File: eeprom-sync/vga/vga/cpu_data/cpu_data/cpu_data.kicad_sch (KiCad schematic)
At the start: 32 parts, among them J1 Conn_02x06_Odd_Even, J10 Conn_01x03_Female, J11 Conn_01x02_Female, J12 Conn_02x05_Odd_Even, J2 Conn_01x02_Female, J3 Conn_01x04_Female, J4 Conn_01x15_Female, J5 Conn_01x15_Female, J6 Conn_02x08_Odd_Even, J7 Conn_01x02_Female, J8 Conn_01x02_Female, J9 Conn_01x08_Female, U1 GAL22V10, U2 74HC14, U3 74LS02, U4 IDT7205L12JG, U5 74LS573

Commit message: routing completed
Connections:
- net CS: now also J1.4 (Pin_4); no longer J1.3 (Pin_3)
- net GND: now also J1.1 (Pin_1), J1.11 (Pin_11), J1.3 (Pin_3), J1.5 (Pin_5), J1.7 (Pin_7), J1.9 (Pin_9); no longer J1.10 (Pin_10), J1.12 (Pin_12), J1.2 (Pin_2), J1.4 (Pin_4), J1.6 (Pin_6), J1.8 (Pin_8)
- net SCLK: now also J1.10 (Pin_10); no longer J1.9 (Pin_9)
- net SIO0: now also J1.12 (Pin_12); no longer J1.11 (Pin_11)
- net SIO1: now also J1.2 (Pin_2); no longer J1.1 (Pin_1)
- net SIO2: now also J1.8 (Pin_8); no longer J1.7 (Pin_7)
- net SIO3: now also J1.6 (Pin_6); no longer J1.5 (Pin_5)
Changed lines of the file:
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@@
   (junction (at 116.84 109.22) (diameter 0) (color 0 0 0 0)
   )
-  (junction (at 13.97 107.95) (diameter 0) (color 0 0 0 0)
+  (junction (at 26.67 107.95) (diameter 0) (color 0 0 0 0)
   )
   (junction (at 167.64 148.59) (diameter 0) (color 0 0 0 0)
@@
   (junction (at 90.17 107.95) (diameter 0) (color 0 0 0 0)
   )
-  (junction (at 13.97 105.41) (diameter 0) (color 0 0 0 0)
-  )
-  (junction (at 13.97 110.49) (diameter 0) (color 0 0 0 0)
+  (junction (at 26.67 105.41) (diameter 0) (color 0 0 0 0)
+  )
+  (junction (at 26.67 110.49) (diameter 0) (color 0 0 0 0)
   )
   (junction (at 200.66 148.59) (diameter 0) (color 0 0 0 0)
   )
-  (junction (at 13.97 115.57) (diameter 0) (color 0 0 0 0)
-  )
-  (junction (at 13.97 113.03) (diameter 0) (color 0 0 0 0)
+  (junction (at 26.67 115.57) (diameter 0) (color 0 0 0 0)
+  )
+  (junction (at 26.67 113.03) (diameter 0) (color 0 0 0 0)
   )
   (junction (at 167.64 143.51) (diameter 0) (color 0 0 0 0)
@@
     (stroke (width 0) (type default) (color 0 0 0 0))
   )
-  (wire (pts (xy 13.97 105.41) (xy 13.97 107.95))
+  (wire (pts (xy 26.67 105.41) (xy 26.67 107.95))
     (stroke (width 0) (type default) (color 0 0 0 0))
   )
@@
     (stroke (width 0) (type default) (color 0 0 0 0))
   )
-  (wire (pts (xy 13.97 110.49) (xy 13.97 113.03))
+  (wire (pts (xy 26.67 110.49) (xy 26.67 113.03))
     (stroke (width 0) (type default) (color 0 0 0 0))
   )
@@
     (stroke (width 0) (type default) (color 0 0 0 0))
   )
-  (wire (pts (xy 13.97 107.95) (xy 13.97 110.49))
+  (wire (pts (xy 26.67 107.95) (xy 26.67 110.49))
     (stroke (width 0) (type default) (color 0 0 0 0))
   )
@@
     (stroke (width 0) (type default) (color 0 0 0 0))
   )
-  (wire (pts (xy 13.97 113.03) (xy 13.97 115.57))
+  (wire (pts (xy 26.67 113.03) (xy 26.67 115.57))
     (stroke (width 0) (type default) (color 0 0 0 0))
   )
@@
     (stroke (width 0) (type default) (color 0 0 0 0))
   )
-  (wire (pts (xy 13.97 102.87) (xy 13.97 105.41))
+  (wire (pts (xy 26.67 102.87) (xy 26.67 105.41))
     (stroke (width 0) (type default) (color 0 0 0 0))
   )
@@
     (effects (font (size 1.27 1.27)) (justify left bottom))
   )
-  (label "SIO0" (at 26.67 115.57 0)
+  (label "SIO0" (at 13.97 115.57 0)
     (effects (font (size 1.27 1.27)) (justify left bottom))
   )
@@
     (effects (font (size 1.27 1.27)) (justify right bottom))
   )
-  (label "SIO2" (at 26.67 110.49 0)
+  (label "SIO2" (at 13.97 110.49 0)
     (effects (font (size 1.27 1.27)) (justify left bottom))
   )
@@
     (effects (font (size 1.27 1.27)) (justify right bottom))
   )
-  (label "SIO1" (at 26.67 102.87 0)
-    (effects (font (size 1.27 1.27)) (justify left bottom))
-  )
-  (label "SCLK" (at 26.67 113.03 0)
+  (label "SIO1" (at 13.97 102.87 0)
+    (effects (font (size 1.27 1.27)) (justify left bottom))
+  )
+  (label "SCLK" (at 13.97 113.03 0)
     (effects (font (size 1.27 1.27)) (justify left bottom))
   )
@@
     (effects (font (size 1.27 1.27)) (justify left bottom))
   )
-  (label "SIO3" (at 26.67 107.95 0)
+  (label "SIO3" (at 13.97 107.95 0)
     (effects (font (size 1.27 1.27)) (justify left bottom))
   )
@@
     (effects (font (size 1.27 1.27)) (justify left bottom))
   )
-  (label "CS" (at 26.67 105.41 0)
+  (label "CS" (at 13.97 105.41 0)
     (effects (font (size 1.27 1.27)) (justify left bottom))
   )
@@
     (pin "2")
   )
-  (symbol (lib_id "power:GND") (at 13.97 115.57 0) (unit 1)
-    (in_bom yes) (on_board yes) (fields_autoplaced)
-    (property "Reference" "#PWR0104" (id 0) (at 13.97 121.92 0)
-      (effects (font (size 1.27 1.27)) hide)
-    )
-    (property "Value" "GND" (id 1) (at 13.97 120.65 0))
-    (property "Footprint" "" (id 2) (at 13.97 115.57 0)
-      (effects (font (size 1.27 1.27)) hide)
-    )
-    (property "Datasheet" "" (id 3) (at 13.97 115.57 0)
-      (effects (font (size 1.27 1.27)) hide)
-    )
+  (symbol (lib_id "power:GND") (at 26.67 115.57 0) (unit 1)
+    (in_bom yes) (on_board yes) (fields_autoplaced)
+    (property "Reference" "#PWR0104" (id 0) (at 26.67 121.92 0)
+      (effects (font (size 1.27 1.27)) hide)
+    )
+    (property "Value" "GND" (id 1) (at 26.67 120.65 0))
+    (property "Footprint" "" (id 2) (at 26.67 115.57 0)
+      (effects (font (size 1.27 1.27)) hide)
+    )
+    (property "Datasheet" "" (id 3) (at 26.67 115.57 0)
+      (effects (font (size 1.27 1.27)) hide)
+    )

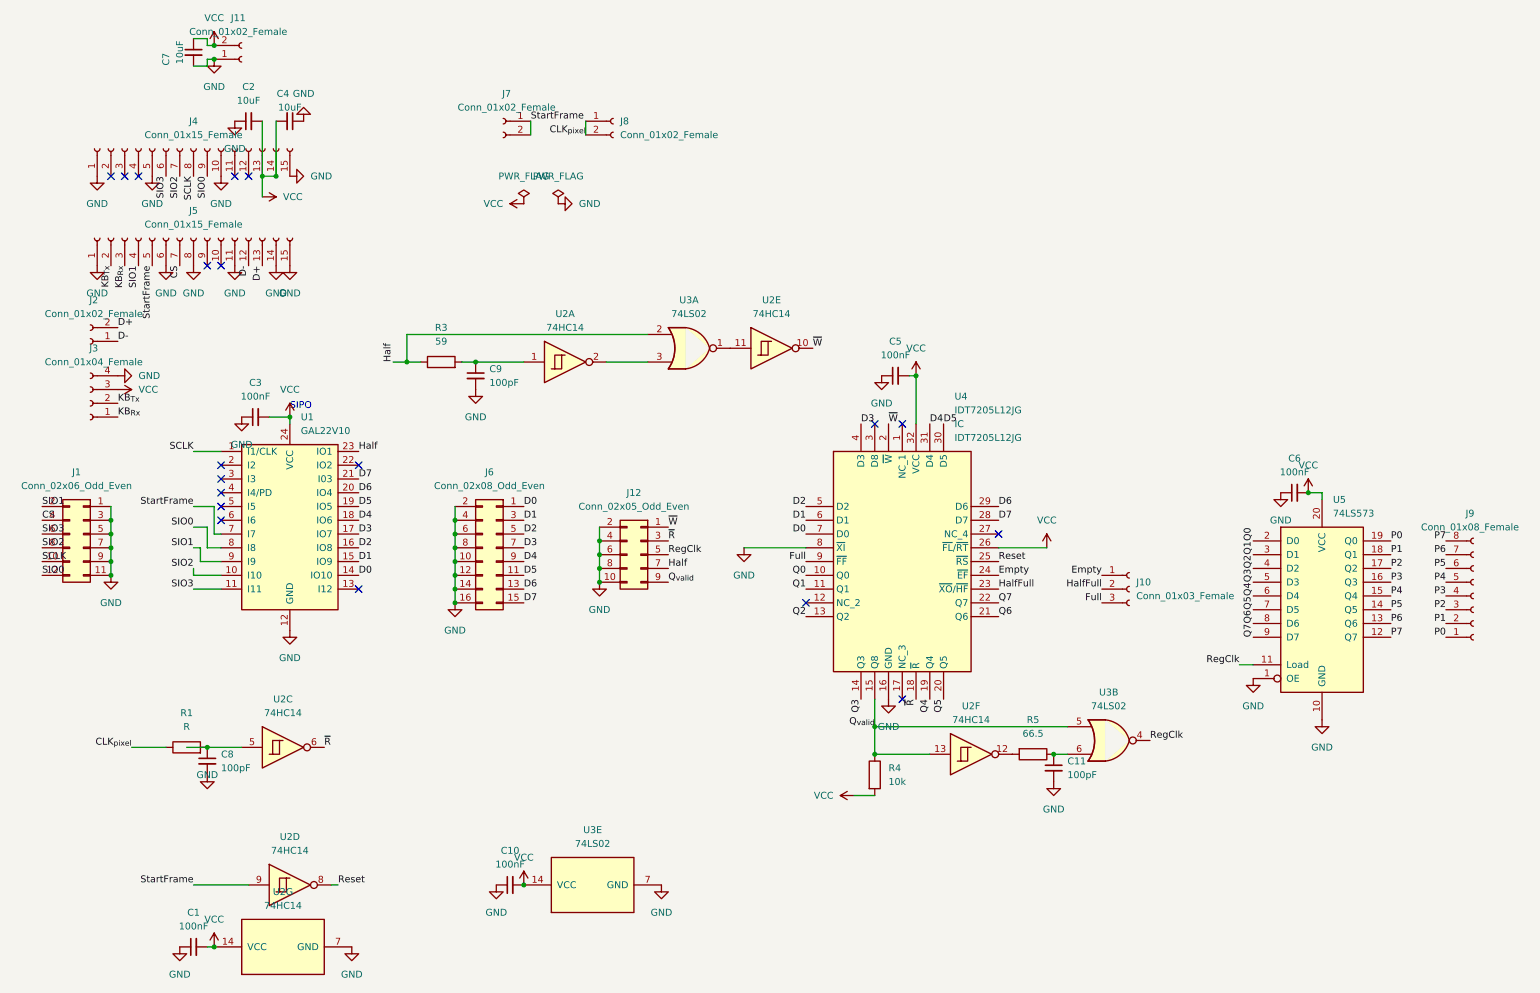
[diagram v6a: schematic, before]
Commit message: labels on the back of the board, layout and retraced, labels on front of board
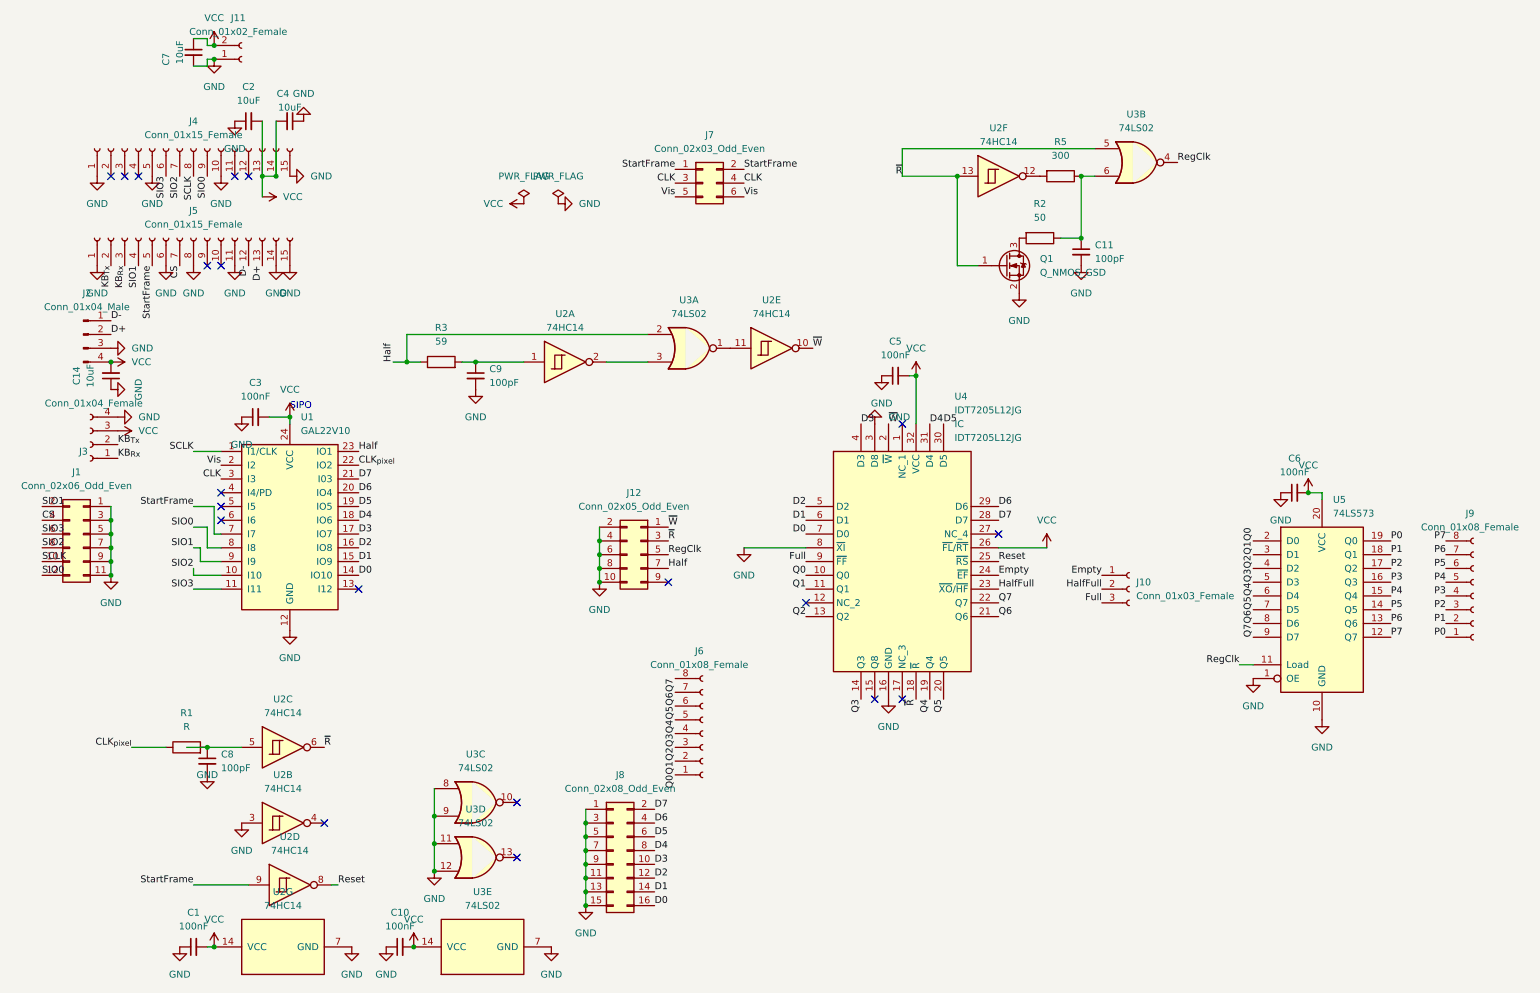
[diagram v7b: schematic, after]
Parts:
- removed J2: Conn_01x02_Female, Connector_PinHeader_2.54mm:PinHeader_1x02_P2.54mm_Vertical, symbol Connector:Conn_01x02_Female
- removed J6: Conn_02x08_Odd_Even, Connector_PinHeader_2.54mm:PinHeader_2x08_P2.54mm_Vertical, symbol Connector_Generic:Conn_02x08_Odd_Even
- removed J7, J8: Conn_01x02_Female, Connector_PinSocket_2.54mm:PinSocket_1x02_P2.54mm_Vertical, symbol Connector:Conn_01x02_Female
- removed R4: 10k, Resistor_SMD:R_0805_2012Metric_Pad1.20x1.40mm_HandSolder, symbol Device:R
- added C14: 10uF, Capacitor_SMD:C_0805_2012Metric_Pad1.18x1.45mm_HandSolder, symbol Device:C_Small
- added J2: Conn_01x04_Male, Connector_PinHeader_2.54mm:PinHeader_1x04_P2.54mm_Vertical, symbol Connector:Conn_01x04_Male
- added J6: Conn_01x08_Female, Connector_PinSocket_2.54mm:PinSocket_1x08_P2.54mm_Vertical, symbol Connector:Conn_01x08_Female
- added J7: Conn_02x03_Odd_Even, Connector_PinSocket_2.54mm:PinSocket_2x03_P2.54mm_Vertical, symbol Connector_Generic:Conn_02x03_Odd_Even
- added J8: Conn_02x08_Odd_Even, Connector_PinHeader_2.54mm:PinHeader_2x08_P2.54mm_Vertical, symbol Connector_Generic:Conn_02x08_Odd_Even
- added Q1: Q_NMOS_GSD, Package_TO_SOT_SMD:SOT-323_SC-70_Handsoldering, symbol Device:Q_NMOS_GSD
- added R2: 50, Resistor_SMD:R_0805_2012Metric_Pad1.20x1.40mm_HandSolder, symbol Device:R
- added unit 2 of U2
- added unit 3 of U3
- added unit 4 of U3
- R5: value 66.5 -> 300
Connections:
- net CLK_{pixel}: now also U1.22 (IO2)
- net D+: now also J2.2 (Pin_2)
- net D-: now also J2.1 (Pin_1)
- net D0: now also J8.16 (Pin_16)
- net D1: now also J8.14 (Pin_14)
- net D2: now also J8.12 (Pin_12)
- net D3: now also J8.10 (Pin_10)
- net D4: now also J8.8 (Pin_8)
- net D5: now also J8.6 (Pin_6)
- net D6: now also J8.4 (Pin_4)
- net D7: now also J8.2 (Pin_2)
- net GND: now also U4.3 (D8), C14.1, J2.3 (Pin_3), J8.1 (Pin_1), J8.11 (Pin_11), J8.13 (Pin_13), J8.15 (Pin_15), J8.3 (Pin_3), J8.5 (Pin_5), J8.7 (Pin_7), J8.9 (Pin_9), Q1.2 (S), U2.3, U3.11, U3.12, U3.8, U3.9
- net Q0: now also J6.1 (Pin_1)
- net Q1: now also J6.2 (Pin_2)
- net Q2: now also J6.3 (Pin_3)
- net Q3: now also J6.4 (Pin_4)
- net Q4: now also J6.5 (Pin_5)
- net Q5: now also J6.6 (Pin_6)
- net Q6: now also J6.7 (Pin_7)
- net Q7: now also J6.8 (Pin_8)
- net StartFrame: now also J7.1 (Pin_1), J7.2 (Pin_2)
- net VCC: now also C14.2, J2.4 (Pin_4)
- net ~{R}: now also U2.13, U3.5, Q1.1 (G)
- net at C11.1, R5.1, U3.6: now also R2.1
- net Vis: now reaches U1.2 (I2)
- net Vis: now also J7.5 (Pin_5), J7.6 (Pin_6)
- net CLK: now reaches U1.3 (I3)
- net CLK: now also J7.3 (Pin_3), J7.4 (Pin_4)
- removed net Q_{valid}: J12.9 (Pin_9), U2.13, U3.5, U4.15 (Q8)
- new net: Q1.3 (D), R2.2
- no-connect marks 19 -> 20
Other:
- moved on the sheet: C10, C11, J3, R5, U2F, U3B, U3E

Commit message: updating gal to include the pixel clk output as expressed in the scchematic
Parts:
- R1: value R -> 34; Tested (none) -> Eric; Updated (none) -> 2023-06-19
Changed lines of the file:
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@@
-    (stroke (width 0) (type default) (color 0 0 0 0))
-  )
-  (wire (pts (xy 40.64 147.32) (xy 44.45 147.32))
     (stroke (width 0) (type default) (color 0 0 0 0))
   )
@@
     (in_bom yes) (on_board yes) (fields_autoplaced)
     (property "Reference" "R1" (id 0) (at 40.64 140.97 90))
-    (property "Value" "R" (id 1) (at 40.64 143.51 90))
+    (property "Value" "34" (id 1) (at 40.64 143.51 90))
     (property "Footprint" "Resistor_SMD:R_0805_2012Metric_Pad1.20x1.40mm_HandSolder" (id 2) (at 40.64 149.098 90)
       (effects (font (size 1.27 1.27)) hide)
     )
     (property "Datasheet" "~" (id 3) (at 40.64 147.32 0)
+      (effects (font (size 1.27 1.27)) hide)
+    )
+    (property "Updated" "2023-06-19" (id 4) (at 40.64 147.32 90)
+      (effects (font (size 1.27 1.27)) hide)
+    )
+    (property "Tested" "Eric" (id 5) (at 40.64 147.32 90)
       (effects (font (size 1.27 1.27)) hide)
     )
@@
   (symbol (lib_id "power:GND") (at 50.8 161.29 0) (unit 1)
     (in_bom yes) (on_board yes) (fields_autoplaced)
-    (property "Reference" "#PWR?" (id 0) (at 50.8 167.64 0)
+    (property "Reference" "#PWR0113" (id 0) (at 50.8 167.64 0)
       (effects (font (size 1.27 1.27)) hide)
     )
@@
   (symbol (lib_id "power:GND") (at 86.36 170.18 0) (unit 1)
     (in_bom yes) (on_board yes) (fields_autoplaced)
-    (property "Reference" "#PWR?" (id 0) (at 86.36 176.53 0)
+    (property "Reference" "#PWR0103" (id 0) (at 86.36 176.53 0)
       (effects (font (size 1.27 1.27)) hide)
     )
@@
       (reference "#PWR0102") (unit 1) (value "GND") (footprint "")
     )
+    (path "/d12d1e25-b6dd-46e0-b703-5f712224d070"
+      (reference "#PWR0103") (unit 1) (value "GND") (footprint "")
+    )
     (path "/a0f9da22-1f8b-45e4-9749-a276c92d0c81"
       (reference "#PWR0104") (unit 1) (value "GND") (footprint "")
@@
     )
     (path "/8624fe9d-9dbf-4cfb-bc83-c0dde04496f2"
-      (reference "#PWR?") (unit 1) (value "GND") (footprint "")
-    )
-    (path "/d12d1e25-b6dd-46e0-b703-5f712224d070"
-      (reference "#PWR?") (unit 1) (value "GND") (footprint "")
+      (reference "#PWR0113") (unit 1) (value "GND") (footprint "")
     )
     (path "/6d97fa49-1c40-4588-b114-7b816ee2ddf7"
@@
     )
     (path "/1d2b3841-519e-4073-a1fd-a33bb4b3d42b"
-      (reference "R1") (unit 1) (value "R") (footprint "Resistor_SMD:R_0805_2012Metric_Pad1.20x1.40mm_HandSolder")
+      (reference "R1") (unit 1) (value "34") (footprint "Resistor_SMD:R_0805_2012Metric_Pad1.20x1.40mm_HandSolder")
     )
     (path "/c965255e-591a-4b5c-884e-517d7797af47"
